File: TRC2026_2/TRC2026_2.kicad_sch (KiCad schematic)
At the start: 32 parts, among them J1 Conn_01x02_Pin, J15 Conn_01x04_Pin, J16 デジタル電圧計(測定), J17 デジタル電圧計(電力供給), J2 Conn_01x04_Pin, J3 Conn_01x04_Pin, J4 Conn_01x04_Pin, J5 Conn_01x04_Pin, J6 Conn_01x04_Pin, SW1 SW_SPST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

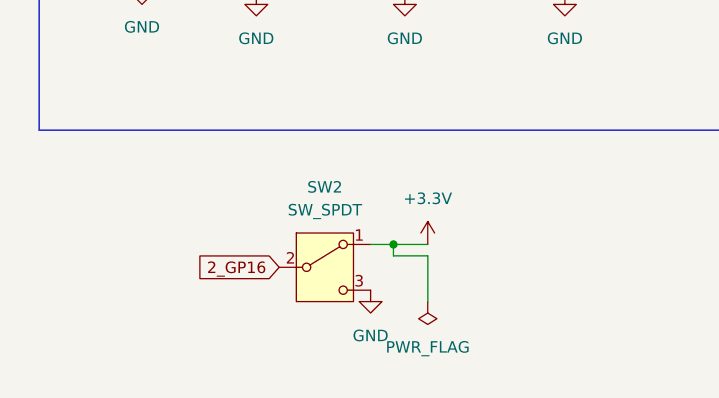
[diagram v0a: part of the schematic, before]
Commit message: プルダウン抵抗とフットプリントを修正しました
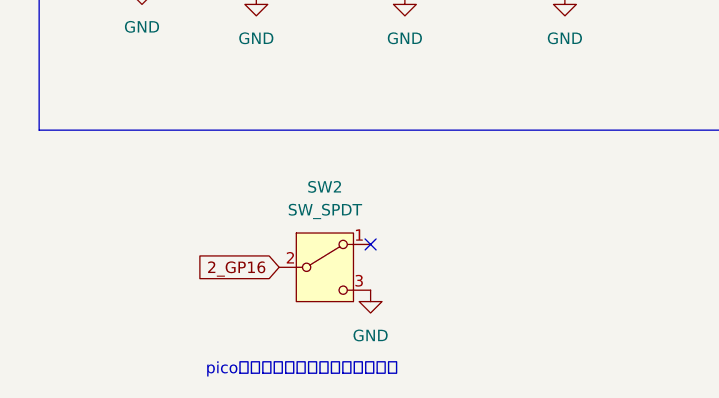
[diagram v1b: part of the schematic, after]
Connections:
- net +3.3V: no longer SW2.1 (A)
- no-connect marks 3 -> 4
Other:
- note added: "picoのプルアップ抵抗をつけること"
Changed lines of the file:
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@@
 	(generator_version "9.0")
 	(paper "A4")
+	(text "picoのプルアップ抵抗をつけること"
+		(exclude_from_sim no)
+		(at 43.18 176.53 0)
+		(effects
+			(font
+				(size 1.27 1.27)
+			)
+		)
+	)
 	(text_box "電源系"
 		(exclude_from_sim no)
@@
 		(color 0 0 0 0)
 	)
-	(junction
-		(at 53.34 162.56)
-		(diameter 0)
-		(color 0 0 0 0)
+	(no_connect
+		(at 50.8 162.56)
 	)
 	(no_connect
@@
 	(wire
 		(pts
-			(xy 57.15 162.56) (xy 53.34 162.56)
-		)
-		(stroke
-			(width 0)
-			(type default)
-		)
-	)
-	(wire
-		(pts
 			(xy 74.93 41.91) (xy 66.04 41.91)
 		)
@@
 	(wire
 		(pts
-			(xy 57.15 163.83) (xy 53.34 163.83)
-		)
-		(stroke
-			(width 0)
-			(type default)
-		)
-	)
-	(wire
-		(pts
 			(xy 31.75 128.27) (xy 31.75 130.81)
 		)
@@
 	(wire
 		(pts
-			(xy 53.34 162.56) (xy 50.8 162.56)
-		)
-		(stroke
-			(width 0)
-			(type default)
-		)
-	)
-	(wire
-		(pts
 			(xy 67.31 81.28) (xy 67.31 83.82)
 		)
@@
 	(wire
 		(pts
-			(xy 53.34 163.83) (xy 53.34 162.56)
-		)
-		(stroke
-			(width 0)
-			(type default)
-		)
-	)
-	(wire
-		(pts
 			(xy 39.37 58.42) (xy 39.37 73.66)
 		)
@@
 	(wire
 		(pts
-			(xy 57.15 168.91) (xy 57.15 163.83)
-		)
-		(stroke
-			(width 0)
-			(type default)
-		)
-	)
-	(wire
-		(pts
 			(xy 133.35 90.17) (xy 125.73 90.17)
 		)
@@
 	)
 	(symbol
-		(lib_id "power:+3.3V")
-		(at 57.15 162.56 0)
-		(unit 1)
-		(exclude_from_sim no)
-		(in_bom yes)
-		(on_board yes)
-		(dnp no)
-		(fields_autoplaced yes)
-		(property "Reference" "#PWR019"
-			(at 57.15 166.37 0)
-			(effects
-				(font
-					(size 1.27 1.27)
-				)
-				(hide yes)
-			)
-		)
-		(property "Value" "+3.3V"
-			(at 57.15 157.48 0)
-			(effects
-				(font
-					(size 1.27 1.27)
-				)
-			)
-		)
-		(property "Footprint" ""
-			(at 57.15 162.56 0)
-			(effects
-				(font
-					(size 1.27 1.27)
-				)
-				(hide yes)
-			)
-		)
-		(property "Datasheet" ""
-			(at 57.15 162.56 0)
-			(effects
-				(font
-					(size 1.27 1.27)
-				)
-				(hide yes)
-			)
-		)
-		(property "Description" "Power symbol creates a global label with name \"+3.3V\""
-			(at 57.15 162.56 0)
-			(effects
-				(font
-					(size 1.27 1.27)
-				)
-				(hide yes)
-			)
-		)
-		(pin "1"
-		)
-		(instances
-			(project ""
-				(path "/9879a251-74b6-4bc2-8c51-a63e732e52e2"
-					(reference "#PWR019")
-					(unit 1)
-				)
-			)
-		)
-	)
-	(symbol
 		(lib_id "MBR3045FCT:MBR3045FCT")
 		(at 57.15 87.63 270)
@@
 					(unit 1)
 				)
-			)
-		)
-	)
-	(symbol
-		(lib_id "power:PWR_FLAG")
-		(at 57.15 168.91 180)
-		(unit 1)
-		(exclude_from_sim no)
-		(in_bom yes)
-		(on_board yes)
-		(dnp no)
-		(fields_autoplaced yes)
-		(property "Reference" "#FLG05"
-			(at 57.15 170.815 0)
-			(effects
-				(font
-					(size 1.27 1.27)
-				)
-				(hide yes)
-			)
-		)
-		(property "Value" "PWR_FLAG"
-			(at 57.15 173.99 0)
-			(effects
-				(font
-					(size 1.27 1.27)
-				)
-			)
-		)
-		(property "Footprint" ""
-			(at 57.15 168.91 0)
-			(effects
-				(font
-					(size 1.27 1.27)
-				)
-				(hide yes)
-			)
-		)
-		(property "Datasheet" "~"
-			(at 57.15 168.91 0)
-			(effects
-				(font
-					(size 1.27 1.27)
-				)
-				(hide yes)
-			)
-		)
-		(property "Description" "Special symbol for telling ERC where power comes from"
-			(at 57.15 168.91 0)
-			(effects
-				(font
-					(size 1.27 1.27)
-				)
-				(hide yes)
-			)
-		)
-		(pin "1"
-		)
-		(instances
-			(project ""
-				(path "/9879a251-74b6-4bc2-8c51-a63e732e52e2"
-					(reference "#FLG05")
-					(unit 1)
-				)
